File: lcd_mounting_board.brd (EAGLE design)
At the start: 100 x 21.1 mm, 6 parts

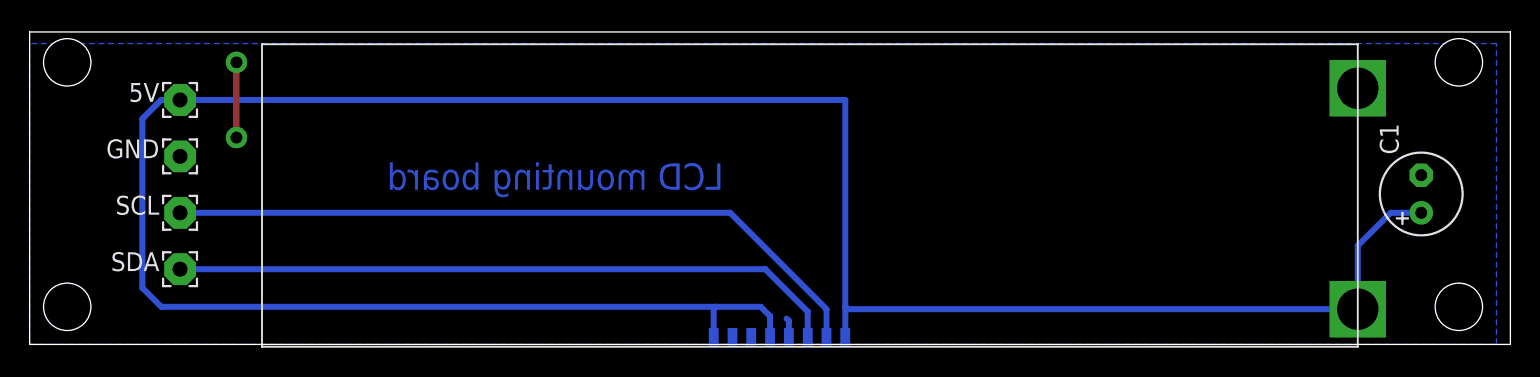
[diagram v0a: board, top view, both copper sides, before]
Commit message: LCD board, moved everything up a bit, for PCB cutting
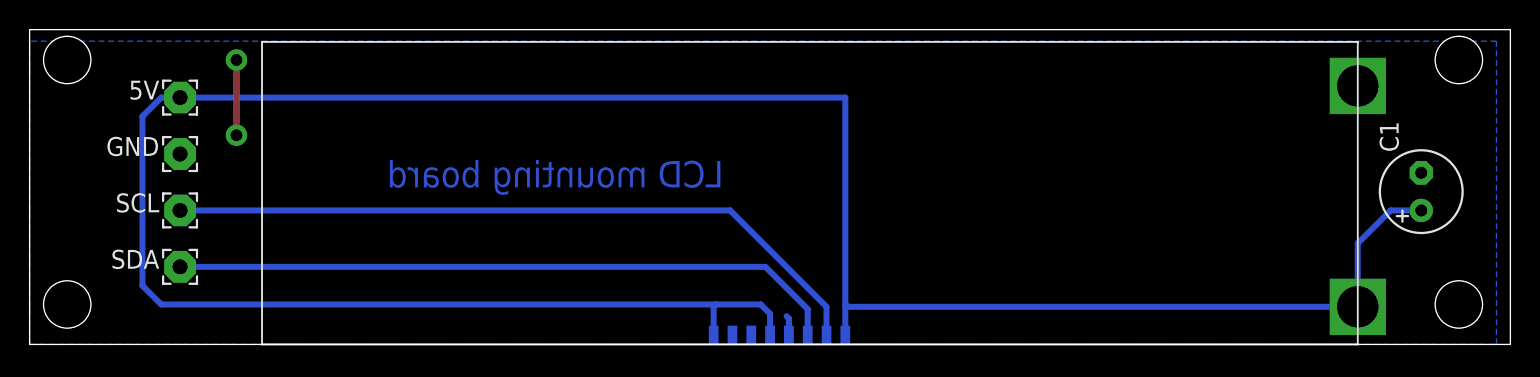
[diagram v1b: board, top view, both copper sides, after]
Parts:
- moved GND 0.16 mm to (10.2, 12.9)
- moved C1 0.16 mm to (94.0, 10.3)
- moved SCL 0.16 mm to (10.2, 9.05)
- moved SDA 0.16 mm to (10.2, 5.24)
- moved U$1 0.16 mm to (54.1, 10.2)
- moved 5V 0.16 mm to (10.2, 16.7)
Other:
- board size 100 x 21.1 mm -> 100 x 21.3 mm
